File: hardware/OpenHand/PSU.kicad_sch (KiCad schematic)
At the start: 31 parts, among them Q3 PMOS, U3 TPS63070RNMR, U4 AMS1117-3.3, U5 LT1175-5_SOT223

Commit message: Update schm and pcb
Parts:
- TP50: footprint (none) -> TestPoint:TestPoint_Pad_D1.0mm
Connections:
- net +5V: no longer U5.2 (IN)
- net +BATT: now also D3.1 (K), Q3.3 (S), U5.2 (IN)

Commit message: update schm and pcb again
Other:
- moved on the sheet: D3
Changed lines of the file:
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@@
   (junction (at 62.865 46.99) (diameter 0) (color 0 0 0 0)
   )
+  (junction (at 46.99 46.99) (diameter 0) (color 0 0 0 0)
+  )
   (junction (at 158.75 82.55) (diameter 0) (color 0 0 0 0)
   )
@@
   (junction (at 223.52 46.99) (diameter 0) (color 0 0 0 0)
   )
-  (junction (at 49.53 46.99) (diameter 0) (color 0 0 0 0)
-  )
   (junction (at 102.87 46.99) (diameter 0) (color 0 0 0 0)
   )
@@
     (stroke (width 0) (type default))
   )
-  (wire (pts (xy 49.53 55.88) (xy 49.53 57.15))
+  (wire (pts (xy 46.99 55.88) (xy 46.99 57.15))
     (stroke (width 0) (type default))
   )
@@
     (stroke (width 0) (type default))
   )
+  (wire (pts (xy 46.99 46.99) (xy 62.865 46.99))
+    (stroke (width 0) (type default))
+  )
   (wire (pts (xy 260.35 46.99) (xy 260.35 50.8))
     (stroke (width 0) (type default))
@@
     (stroke (width 0) (type default))
   )
-  (wire (pts (xy 44.45 46.99) (xy 49.53 46.99))
+  (wire (pts (xy 44.45 46.99) (xy 46.99 46.99))
     (stroke (width 0) (type default))
   )
@@
     (stroke (width 0) (type default))
   )
-  (wire (pts (xy 49.53 57.15) (xy 39.37 57.15))
+  (wire (pts (xy 46.99 57.15) (xy 39.37 57.15))
     (stroke (width 0) (type default))
   )
@@
     (stroke (width 0) (type default))
   )
-  (wire (pts (xy 49.53 46.99) (xy 62.865 46.99))
-    (stroke (width 0) (type default))
-  )
   (wire (pts (xy 234.95 57.15) (xy 234.95 59.69))
     (stroke (width 0) (type default))
@@
     (stroke (width 0) (type default))
   )
-  (wire (pts (xy 49.53 48.26) (xy 49.53 46.99))
+  (wire (pts (xy 46.99 48.26) (xy 46.99 46.99))
     (stroke (width 0) (type default))
   )
@@
     )
   )
-  (symbol (lib_id "Device:D_Zener") (at 49.53 52.07 270) (unit 1)
-    (in_bom yes) (on_board yes) (dnp no) (fields_autoplaced)
-    (property "Reference" "D3" (at 52.07 50.8 90)
-      (effects (font (size 1.27 1.27)) (justify left))
-    )
-    (property "Value" "5V Zener" (at 52.07 53.34 90)
-      (effects (font (size 1.27 1.27)) (justify left))
-    )
-    (property "Footprint" "Diode_THT:D_A-405_P7.62mm_Horizontal" (at 49.53 52.07 0)
-      (effects (font (size 1.27 1.27)) hide)
-    )
-    (property "Datasheet" "~" (at 49.53 52.07 0)
+  (symbol (lib_id "Device:D_Zener") (at 46.99 52.07 270) (unit 1)
+    (in_bom yes) (on_board yes) (dnp no) (fields_autoplaced)
+    (property "Reference" "D3" (at 49.53 50.8 90)
+      (effects (font (size 1.27 1.27)) (justify left))
+    )
+    (property "Value" "5V Zener" (at 49.53 53.34 90)
+      (effects (font (size 1.27 1.27)) (justify left))
+    )
+    (property "Footprint" "Diode_THT:D_A-405_P7.62mm_Horizontal" (at 46.99 52.07 0)
+      (effects (font (size 1.27 1.27)) hide)
+    )
+    (property "Datasheet" "~" (at 46.99 52.07 0)
       (effects (font (size 1.27 1.27)) hide)
     )
@@
         )
         (path "/f1fbd835-8408-4592-854c-2fbec9d052ec/11b37193-b902-4bf9-977f-96c37af6f134"
-          (reference "TP38") (unit 1)
+          (reference "TP34") (unit 1)
         )
       )
@@
         )
         (path "/f1fbd835-8408-4592-854c-2fbec9d052ec/11b37193-b902-4bf9-977f-96c37af6f134"
-          (reference "TP33") (unit 1)
+          (reference "TP29") (unit 1)
         )
       )
@@
         )
         (path "/f1fbd835-8408-4592-854c-2fbec9d052ec/11b37193-b902-4bf9-977f-96c37af6f134"
-          (reference "TP35") (unit 1)
+          (reference "TP31") (unit 1)
         )
       )
@@
         )
         (path "/f1fbd835-8408-4592-854c-2fbec9d052ec/11b37193-b902-4bf9-977f-96c37af6f134"
-          (reference "TP34") (unit 1)
+          (reference "TP30") (unit 1)
         )
       )
@@
         )
         (path "/f1fbd835-8408-4592-854c-2fbec9d052ec/11b37193-b902-4bf9-977f-96c37af6f134"
-          (reference "TP36") (unit 1)
+          (reference "TP32") (unit 1)
         )
       )
@@
         )
         (path "/f1fbd835-8408-4592-854c-2fbec9d052ec/11b37193-b902-4bf9-977f-96c37af6f134"
-          (reference "TP37") (unit 1)
-        )
-      )
+          (reference "TP33") (unit 1)
+        )
+      )

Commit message: Major updates to schm and pcb, a bit better design
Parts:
- removed C12: 100n, Capacitor_SMD:C_1206_3216Metric_Pad1.33x1.80mm_HandSolder, symbol Device:C
- removed C5: 10u, Capacitor_SMD:C_0805_2012Metric_Pad1.18x1.45mm_HandSolder, symbol Device:C
- removed JP23: JMPR_REVP, Jumper:SolderJumper-2_P1.3mm_Bridged_RoundedPad1.0x1.5mm, symbol Jumper:SolderJumper_2_Bridged
- removed JP24: JMPR_PSU, Jumper:SolderJumper-2_P1.3mm_Bridged_RoundedPad1.0x1.5mm, symbol Jumper:SolderJumper_2_Bridged
- removed Q3: PMOS, Package_DIP:Vishay_HVM-DIP-3_W7.62mm, symbol Simulation_SPICE:PMOS
- removed R16: 10k, Resistor_SMD:R_0805_2012Metric_Pad1.20x1.40mm_HandSolder, symbol Device:R
- removed R18: 100k, Resistor_SMD:R_0805_2012Metric_Pad1.20x1.40mm_HandSolder, symbol Device:R
- removed R20: 130k, Resistor_SMD:R_0805_2012Metric_Pad1.20x1.40mm_HandSolder, symbol Device:R
- removed TP50: TP_PSU_FDBK, TestPoint:TestPoint_Pad_D1.0mm, symbol Connector:TestPoint_Small
- removed U3: TPS63070RNMR, TPS63070RNMR:TPS63070RNMR, symbol TPS63070RNMR:TPS63070RNMR
- added C10: 100n, Capacitor_SMD:C_0805_2012Metric, symbol Device:C
- added Q1: AO3401A, Package_TO_SOT_SMD:SOT-23, symbol Transistor_FET:AO3401A
- added R9: 54.9k, Resistor_SMD:R_0805_2012Metric, symbol Device:R
- added R9: 10k, Resistor_SMD:R_0805_2012Metric, symbol Device:R
- added U2: TPS565201DDCR, TPS565201DDCR:TPS565201DDCR_L, symbol TPS565201DDCR:TPS565201DDCR
- C11: renamed from C6; footprint Capacitor_SMD:C_0805_2012Metric_Pad1.18x1.45mm_HandSolder -> Capacitor_SMD:C_0805_2012Metric; Package 0805 -> (none)
- C12: renamed from C7; footprint Capacitor_SMD:C_0805_2012Metric_Pad1.18x1.45mm_HandSolder -> Capacitor_SMD:C_0805_2012Metric; Package 0805 -> (none)
- C13: renamed from C8; value 22u -> 1u; footprint Capacitor_SMD:C_0805_2012Metric_Pad1.18x1.45mm_HandSolder -> Capacitor_SMD:C_0805_2012Metric; Package 0805 -> (none)
- C14: renamed from C13; footprint Capacitor_SMD:C_0805_2012Metric_Pad1.18x1.45mm_HandSolder -> Capacitor_SMD:C_0805_2012Metric; Package 0805 -> (none)
- C15: renamed from C14; footprint Capacitor_SMD:C_0805_2012Metric_Pad1.18x1.45mm_HandSolder -> Capacitor_SMD:C_0805_2012Metric; Package 0805 -> (none)
- C7: renamed from C9; footprint Capacitor_SMD:C_0805_2012Metric_Pad1.18x1.45mm_HandSolder -> Capacitor_SMD:C_0805_2012Metric; Package 0805 -> (none)
- C8: renamed from C10; footprint Capacitor_SMD:C_0805_2012Metric_Pad1.18x1.45mm_HandSolder -> Capacitor_SMD:C_0805_2012Metric; Package 0805 -> (none)
- C9: renamed from C11; value 10u -> 100n; footprint Capacitor_SMD:C_0805_2012Metric_Pad1.18x1.45mm_HandSolder -> Capacitor_SMD:C_0805_2012Metric; Package 0603 -> (none)
- D1: footprint LED_SMD:LED_0805_2012Metric -> LED_SMD:LED_1210_3225Metric
- D3: footprint Diode_THT:D_A-405_P7.62mm_Horizontal -> Diode_SMD:D_SOD-123; Part Number (none) -> BZT52C4V7
- L1: value 1.5uH -> 3.3uH; footprint Inductor_THT:L_Radial_D6.0mm_P4.00mm -> Inductor_SMD:L_Bourns_SRP7028A_7.3x6.6mm; Part Number (none) -> CYA0650-3.3UH
- R17: value 680k -> 10k; footprint Resistor_SMD:R_0805_2012Metric_Pad1.20x1.40mm_HandSolder -> Resistor_SMD:R_0805_2012Metric
- R19, R9: footprint Resistor_SMD:R_0805_2012Metric_Pad1.20x1.40mm_HandSolder -> Resistor_SMD:R_0805_2012Metric
- renumbered U4 to U3, U5 to U4
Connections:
- net +5V: now also L1.2, R9.1
- net +BATT: now also R17.2, Q1.2 (S), U2.3 (VIN)
- net BAT_P: now also Q1.3 (D)
- net Earth: now also R9.2, U2.1 (GND)
- net at D3.2 (A), R19.2: now also Q1.1 (G)
- net at R17.1: now also U2.5 (EN)
- net at L1.1: now also C10.1, U2.2 (SW)
- new net: R9.1, R9.2, U2.4 (VFB)
- new net: C10.2, U2.6 (VBST)
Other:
- note added: "Filtering capacitors"
- note added: "PWR LED"
- note added: "TPS565201DDCR switch mode buck converter"
- note removed: "High current SMPS for driving motors"
- note removed: "See datasheet Table 4. for feedback resistor selection (for 5V output)"
- note removed: "TPS63070RNMR switch mode buck converter"
- note removed: "XR XR6*8-2R2M-L Package: Plugin,D6xL8mm"
- moved on the sheet: C11, C12, C13, C14, C7, C8, C9, D1, D3, R19, R9, TP50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

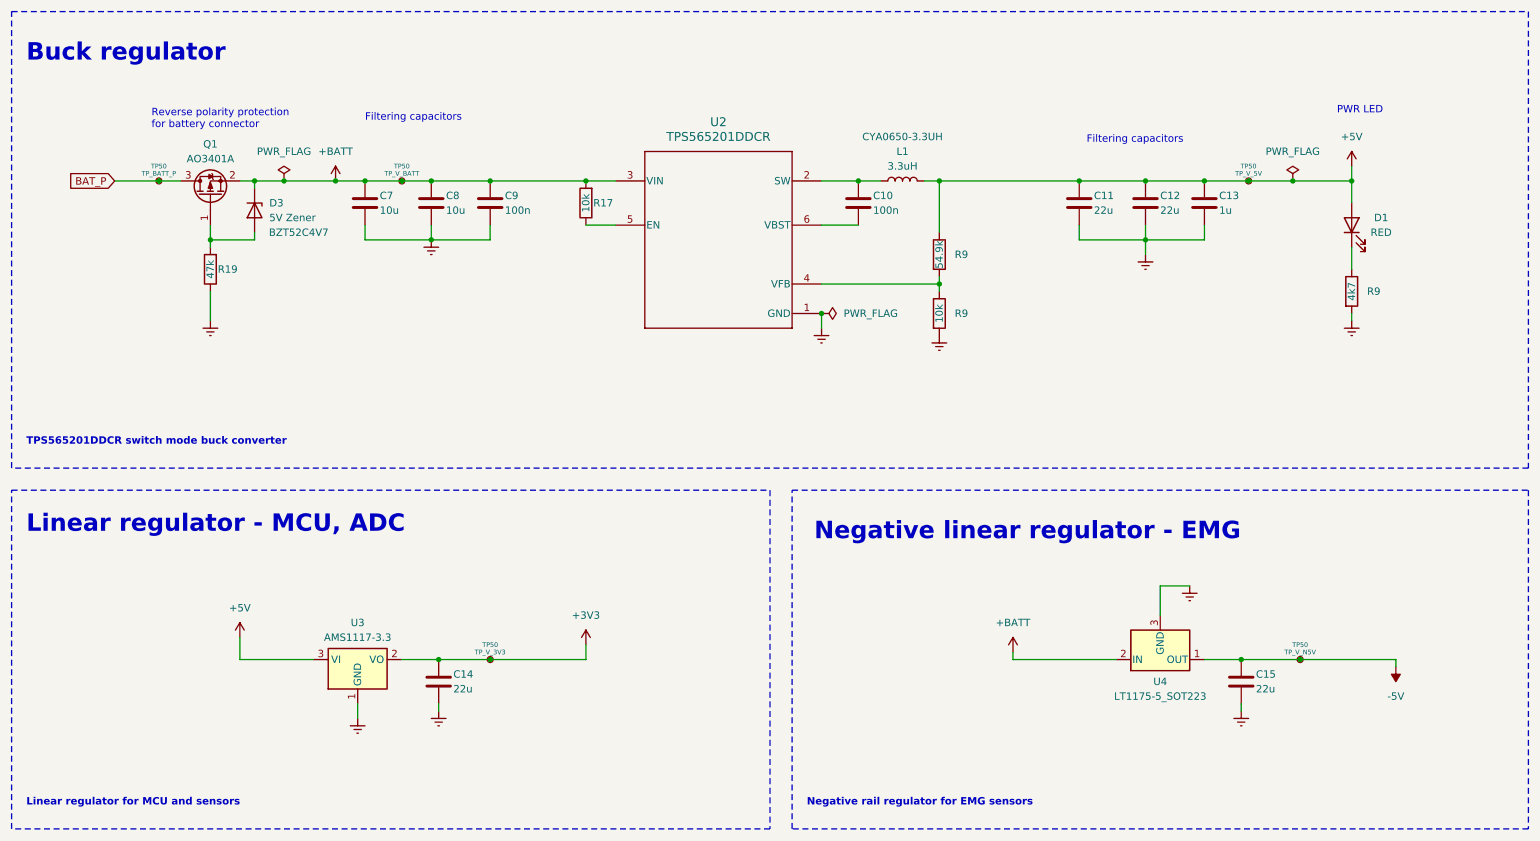
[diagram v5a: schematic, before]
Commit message: Update to KiCAD 8 and order components from LCSC
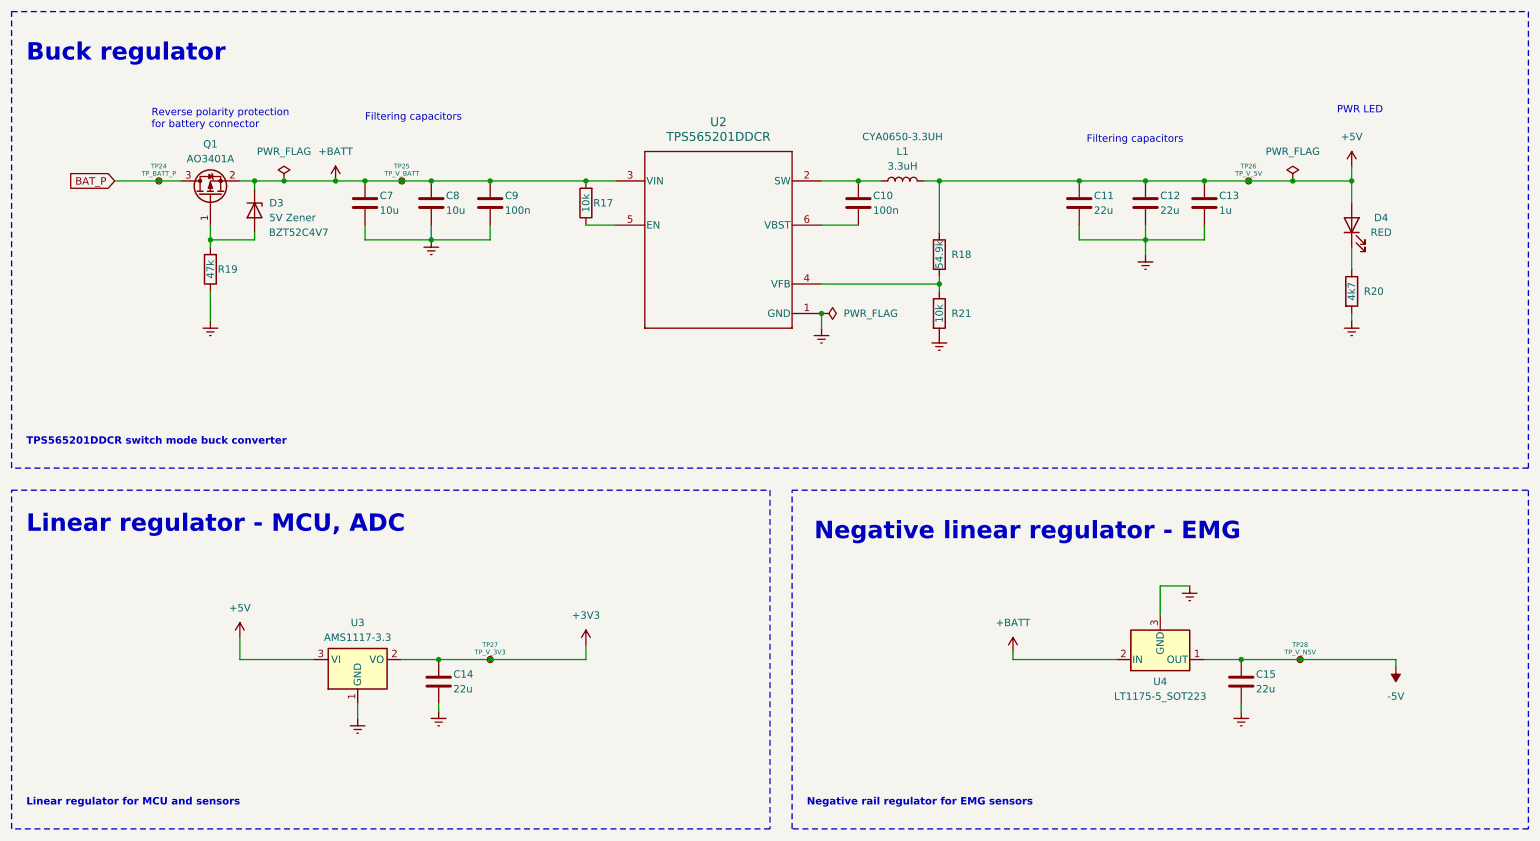
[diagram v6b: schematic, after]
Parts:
- renumbered D1 to D4, R9 to R18, R9 to R20, R9 to R21, TP50 to TP24, TP50 to TP25, TP50 to TP26, TP50 to TP27, TP50 to TP28
